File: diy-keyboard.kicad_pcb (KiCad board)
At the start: 2 copper layers, 157 parts, among them J1 AVR-ISP-6, SW1 ESC, SW10 #9, SW11 #0, SW12 -_, SW13 =+, SW14 BCKSPC, SW15 DEL, SW16 TAB, SW17 Q, SW18 W, SW19 E, SW2 #1, SW20 R, SW21 T, SW22 Y, SW23 U, SW24 I, SW25 O, SW26 P, SW27 [{, SW28 ]}, SW29 \|, SW3 #2, SW30 PGUP, SW31 CPSLCK, SW32 A, SW33 S, SW34 D, SW35 F, SW36 G, SW37 H, SW38 J, SW39 K, SW4 #3, SW40 L, SW41 ;:, SW42 '", SW43 ENTR, SW44 PGDN, SW45 LSHFT, SW46 Z, SW47 X, SW48 C, SW49 V, SW5 #4, SW50 B, SW51 N, SW52 M, SW53 ,<, SW54 .>, SW55 /?, SW56 RSHFT, SW57 UP, SW58 INS, SW59 LCTRL, SW6 #5, SW60 SUPER, SW61 LALT, SW62 SPACE, SW63 RALT, SW64 Fn, SW65 RCTRL, SW66 LEFT, SW67 DOWN, SW68 RIGHT, SW69 SW_SKQG, SW7 #6, SW8 #7, SW9 #8, U1 PRTR5V0U2X, U2 ATmega32U4-A, Y1 16MHz

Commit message: Making edge cuts PCB taking a shape
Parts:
- SW69: footprint Button_Switch_SMD:SW_SPST_SKQG_WithoutStem -> Button_Switch_SMD:SW_SPST_SKQG_WithStem
- moved R3 70.1 mm to (153.3, 150.4)
- moved SW69 60.6 mm to (155.4, 155.8)
- moved C7 57.3 mm to (209.2, 149.8), turned to 90 degrees
- moved C5 46.5 mm to (203.5, 148.3), turned to 0 degrees
- moved J1 44.9 mm to (166.5, 155.6)
- moved C4 43.6 mm to (191.9, 151.5), turned to -90 degrees
- moved C6 37.8 mm to (204.2, 164.3), turned to 0 degrees
- moved R6 28.8 mm to (191.0, 162.3)
- moved C8 15.2 mm to (192.7, 148.3)
- moved R5 15.1 mm to (198.9, 146.5)
- moved R4 15.1 mm to (196.9, 146.5)
- moved U2 15.1 mm to (199.9, 156.3)
- moved C2 14.6 mm to (216.6, 154.5)
- moved C1 14.6 mm to (216.6, 156.9)
- moved Y1 14.0 mm to (212.0, 155.9)
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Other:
- board outline added: 304.8 x 98.8 mm

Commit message: Routing switch and diode
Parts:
- added REF**: Stabilizer_Cherry_MX_2.00u, Mounting_Keyboard_Stabilizer:Stabilizer_Cherry_MX_2.00u, F.Cu at (323.1, 81.0)
- added REF**: Stabilizer_Cherry_MX_2.00u, Mounting_Keyboard_Stabilizer:Stabilizer_Cherry_MX_2.00u, F.Cu at (77.8, 138.1)
- added REF**: Stabilizer_Cherry_MX_2.00u, Mounting_Keyboard_Stabilizer:Stabilizer_Cherry_MX_2.00u, F.Cu at (320.7, 119.1)
- added REF**: Stabilizer_Cherry_MX_6.25u, Mounting_Keyboard_Stabilizer:Stabilizer_Cherry_MX_6.25u, F.Cu at (180.2, 157.2)
- moved D8 8.92 mm to (193.9, 84.8)
- moved F1 4.17 mm to (204.6, 86.3), turned to -90 degrees
- moved U1 2.29 mm to (208.7, 84.3)
- moved R2 1.54 mm to (206.2, 79.0)
- moved R1 1.07 mm to (210.9, 79.0)
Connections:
- R4 pad 1: Net-(R4-Pad1) -> /DN
- R4 pad 2: Net-(R4-Pad2) -> /DN
- R5 pad 1: Net-(R5-Pad1) -> /DP
- R5 pad 2: Net-(R5-Pad2) -> /DP
- U1 pad 2: Net-(R5-Pad1) -> /DP
- U1 pad 3: Net-(R4-Pad1) -> /DN
- U2 pad 3: Net-(R4-Pad2) -> /DN
- U2 pad 4: Net-(R5-Pad2) -> /DP
- USB1 pad 5: Net-(R4-Pad1) -> /DN
- USB1 pad 6: Net-(R5-Pad1) -> /DP
- USB1 pad 7: Net-(R4-Pad1) -> /DN
- USB1 pad 8: Net-(R5-Pad1) -> /DP
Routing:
- net /ROW0: track 0.00 -> 292.7 mm, vias 0 -> 2
- net /ROW1: track 0.00 -> 290.3 mm, vias 0 -> 2
- net /ROW2: track 0.00 -> 287.7 mm, vias 0 -> 2
- net /ROW3: track 0.00 -> 281.0 mm, vias 0 -> 2
- net /ROW4: track 0.00 -> 214.2 mm
- net /COL6: track 0.00 -> 108.4 mm
- net /COL1: track 0.00 -> 100.9 mm
- net /COL2: track 0.00 -> 99.6 mm
- net /DN: track 0.00 -> 89.8 mm
- net /COL9: track 0.00 -> 89.5 mm
- net /COL10: track 0.00 -> 88.6 mm
- net /DP: track 0.00 -> 88.4 mm
- net /COL13: track 0.00 -> 87.1 mm
- net /COL0: track 0.00 -> 85.6 mm
- net /COL12: track 0.00 -> 84.1 mm
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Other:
- board size 304.8 x 98.8 mm -> 304.8 x 99.9 mm

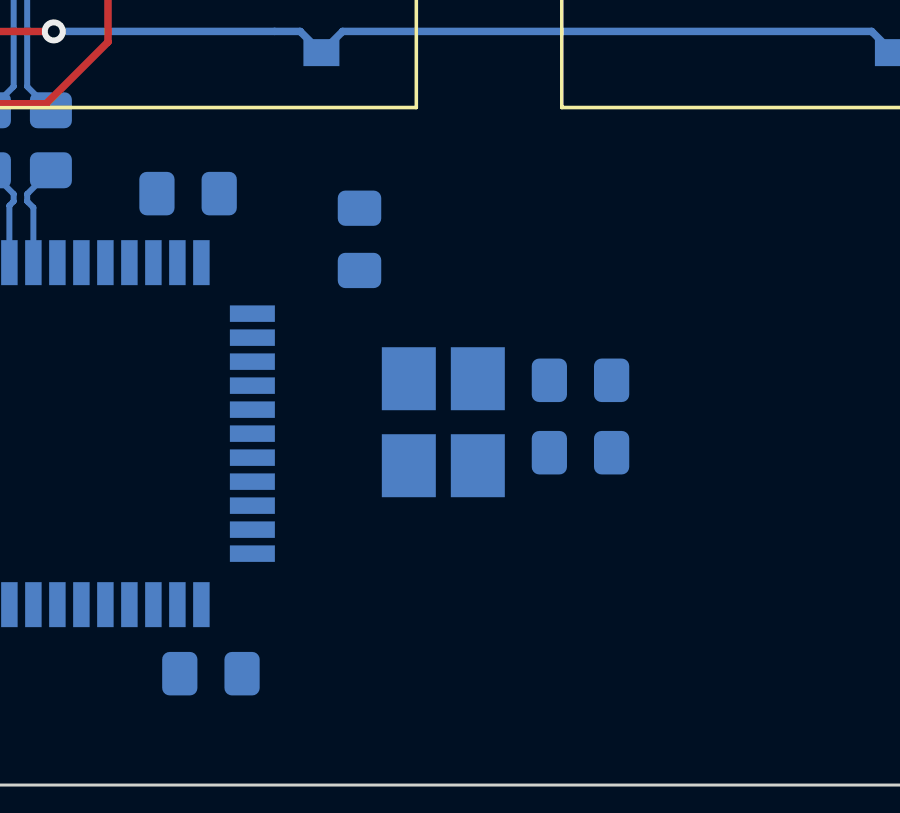
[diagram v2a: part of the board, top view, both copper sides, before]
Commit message: Routing USB and Crystal Oscillator
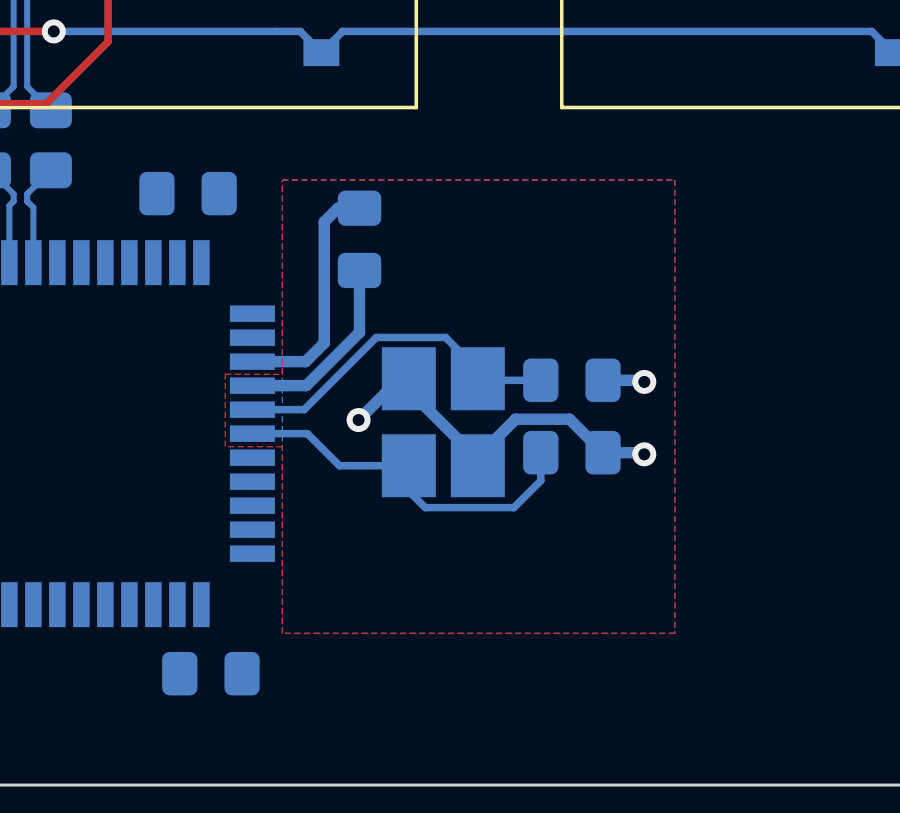
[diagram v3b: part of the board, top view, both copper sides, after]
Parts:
- moved C1 0.29 mm to (216.3, 156.9)
- moved C2 0.29 mm to (216.3, 154.5)
- turned C7 to -90 degrees
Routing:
- net GND: track 0.00 -> 21.0 mm, vias 0 -> 3
- net Net-(C1-Pad1): track 0.00 -> 12.4 mm
- net Net-(C2-Pad1): track 0.00 -> 11.4 mm
- net +5V: track 0.00 -> 8.05 mm
- added copper zone on B.Cu, net GND
- added copper zone on F.Cu, net GND

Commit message: Reassign footprint SW59 and re-allign keyboard layout
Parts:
- SW59: footprint Switch_Keyboard_Cherry_MX:SW_Cherry_MX_PCB_1.25u -> Switch_Keyboard_Cherry_MX:SW_Cherry_MX_PCB_1.50u
- SW63: footprint Switch_Keyboard_Cherry_MX:SW_Cherry_MX_PCB_1.25u -> Switch_Keyboard_Cherry_MX:SW_Cherry_MX_PCB_1.00u
- moved SW69 71.3 mm to (226.6, 152.9)
- moved R3 65.8 mm to (219.1, 151.0)
- moved R6 7.42 mm to (198.2, 164.3)
- moved C6 6.23 mm to (210.5, 164.5)
- moved C3 5.99 mm to (195.6, 161.3), turned to 180 degrees
- moved C7 5.60 mm to (214.7, 151.0), turned to 0 degrees
- moved D61 5.56 mm to (118.2, 161.2)
- moved D60 5.51 mm to (99.1, 161.2)
- moved D62 5.50 mm to (189.3, 161.1)
- moved REF** 4.77 mm to (184.9, 157.4)
- moved SW60 4.76 mm to (94.5, 157.4)
- moved SW61 4.76 mm to (113.5, 157.4)
- moved SW62 4.76 mm to (184.9, 157.4)
- moved R5 4.48 mm to (203.4, 147.1)
- moved R4 4.48 mm to (201.3, 147.1)
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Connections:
- R4 pad 2: /DN -> /D-
- R5 pad 2: /DP -> /D+
- U2 pad 3: /DN -> /D-
- U2 pad 36: /COL6 -> /ROW4
- U2 pad 37: /COL5 -> /COL6
- U2 pad 38: /ROW1 -> /COL5
- U2 pad 39: /ROW4 -> /ROW3
- U2 pad 4: /DP -> /D+
- U2 pad 40: /ROW3 -> /ROW2
- U2 pad 41: /ROW2 -> /ROW1
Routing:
- net /ROW4: track 214.2 -> 296.7 mm, vias 0 -> 2
- net /DP: track 88.4 -> 12.9 mm
- net /DN: track 89.8 -> 14.5 mm
- net GND: track 21.0 -> 93.8 mm, vias 3 -> 0
- net /RESET: track 0.00 -> 25.3 mm
- net /COL1: track 100.9 -> 88.9 mm
- net /COL2: track 99.6 -> 88.9 mm
- net Net-(C2-Pad1): track 11.4 -> 2.05 mm
- net +5V: track 8.05 -> 16.7 mm
- net /ROW0: track 292.7 -> 300.8 mm
- net /COL14: track 78.3 -> 71.1 mm
- net Net-(C1-Pad1): track 12.4 -> 5.86 mm
- net /ROW3: track 281.0 -> 286.2 mm
- net /COL9: track 89.5 -> 85.0 mm
- net /COL0: track 85.6 -> 81.0 mm
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- removed copper zone on B.Cu, net GND
- removed copper zone on F.Cu, net GND

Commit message: Change diode footprint to 1N4148 SOD-123 and re-routing PCB
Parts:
- removed REF** (x3): Stabilizer_Cherry_MX_2.00u, Mounting_Keyboard_Stabilizer:Stabilizer_Cherry_MX_2.00u
- removed REF**: Stabilizer_Cherry_MX_6.25u, Mounting_Keyboard_Stabilizer:Stabilizer_Cherry_MX_6.25u
- added H1: MountingHole, Local_lib_Mounting_Keyboard_Stabilizer:Stabilizer_Cherry_MX_6.25u, F.Cu at (182.6, 165.1)
- added H2: MountingHole, Local_lib_Mounting_Keyboard_Stabilizer:Stabilizer_Cherry_MX_2.00u, F.Cu at (320.6, 88.9)
- added H3: MountingHole, Local_lib_Mounting_Keyboard_Stabilizer:Stabilizer_Cherry_MX_2.00u, F.Cu at (318.3, 127.0)
- added H4: MountingHole, Local_lib_Mounting_Keyboard_Stabilizer:Stabilizer_Cherry_MX_2.00u, F.Cu at (75.4, 146.1)
- D1, D10, D11, D12, D13, D14, D15, D16, D17, D18, D19, D2, D20, D21, D22, D23, D24, D25, D26, D27, D28, D29, D3, D30, D31, D32, D33, D34, D35, D36, D37, D38, D39, D4, D40, D41, D42, D43, D44, D45, D46, D47, D48, D49, D5, D50, D51, D52, D53, D54, D55, D56, D57, D58, D59, D6, D60, D61, D62, D63, D64, D65, D66, D67, D68, D7, D8, D9: value D -> 1N4148W
- J1: footprint ISP-header:Reset_Pretty-Mask -> Local_lib_ISP-header:Reset_Pretty-Mask; moved to F.Cu
- SW1, SW10, SW11, SW12, SW13, SW15, SW17, SW18, SW19, SW2, SW20, SW21, SW22, SW23, SW24, SW25, SW26, SW27, SW28, SW3, SW30, SW32, SW33, SW34, SW35, SW36, SW37, SW38, SW39, SW4, SW40, SW41, SW42, SW44, SW46, SW47, SW48, SW49, SW5, SW50, SW51, SW52, SW53, SW54, SW55, SW57, SW58, SW6, SW60, SW61, SW63, SW64, SW65, SW66, SW67, SW68, SW7, SW8, SW9: footprint Switch_Keyboard_Cherry_MX:SW_Cherry_MX_PCB_1.00u -> Local_lib_Switch_Keyboard_Cherry_MX:SW_Cherry_MX_PCB_1.00u
- SW14: footprint Switch_Keyboard_Cherry_MX:SW_Cherry_MX_PCB_2.00u -> Local_lib_Switch_Keyboard_Cherry_MX:SW_Cherry_MX_PCB_2.00u
- SW16, SW29, SW59: footprint Switch_Keyboard_Cherry_MX:SW_Cherry_MX_PCB_1.50u -> Local_lib_Switch_Keyboard_Cherry_MX:SW_Cherry_MX_PCB_1.50u
- SW31, SW56: footprint Switch_Keyboard_Cherry_MX:SW_Cherry_MX_PCB_1.75u -> Local_lib_Switch_Keyboard_Cherry_MX:SW_Cherry_MX_PCB_1.75u
- SW43, SW45: footprint Switch_Keyboard_Cherry_MX:SW_Cherry_MX_PCB_2.25u -> Local_lib_Switch_Keyboard_Cherry_MX:SW_Cherry_MX_PCB_2.25u
- SW62: footprint Switch_Keyboard_Cherry_MX:SW_Cherry_MX_PCB_6.50u -> Local_lib_Switch_Keyboard_Cherry_MX:SW_Cherry_MX_PCB_6.50u
- U1: footprint Package_TO_SOT_SMD:SOT-143_Handsoldering -> Package_TO_SOT_SMD:SOT-143
- USB1: footprint Type-C:HRO-TYPE-C-31-M-12-HandSoldering -> Local_lib_Type-C:HRO-TYPE-C-31-M-12-HandSoldering
- moved J1 70.5 mm to (240.4, 163.7), turned to 0 degrees
- moved C7 25.7 mm to (191.0, 161.0), turned to 180 degrees
- moved C4 23.6 mm to (205.6, 173.5)
- moved R1 23.0 mm to (189.4, 86.9), turned to -90 degrees
- moved U1 22.5 mm to (187.3, 91.3)
- moved R2 22.5 mm to (184.9, 86.0)
- moved USB1 22.3 mm to (187.3, 73.3)
- moved F1 22.0 mm to (183.5, 92.7)
- moved D7 13.7 mm to (172.7, 92.8)
- moved SW69 13.3 mm to (224.2, 166.0)
- moved R3 11.4 mm to (221.7, 162.1)
- moved C1 11.1 mm to (215.4, 167.6)
- moved Y1 10.7 mm to (211.1, 166.1)
- moved C2 10.7 mm to (215.4, 164.7)
- moved D8 10.6 mm to (200.8, 92.8)
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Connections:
- U2 pad 1: /ROW0 -> /COL5
- U2 pad 38: /COL5 -> /ROW0
- U2 pad 39: /ROW3 -> /ROW1
- U2 pad 41: /ROW1 -> /ROW3
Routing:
- net /ROW0: track 300.8 -> 500.6 mm
- net GND: track 93.8 -> 281.6 mm, vias 0 -> 42
- net /ROW1: track 293.9 -> 480.1 mm
- net +5V: track 16.7 -> 191.9 mm, vias 0 -> 9
- net /COL14: track 71.1 -> 228.8 mm, vias 0 -> 1
- net /ROW2: track 291.9 -> 448.4 mm
- net /COL0: track 81.0 -> 227.8 mm, vias 0 -> 1
- net /COL13: track 82.6 -> 219.8 mm, vias 0 -> 1
- net /COL1: track 88.9 -> 209.8 mm, vias 0 -> 1
- net /COL12: track 81.4 -> 199.1 mm, vias 0 -> 1
- net /COL2: track 88.9 -> 188.5 mm, vias 0 -> 1
- net /COL11: track 81.4 -> 173.7 mm, vias 0 -> 1
- net /COL3: track 64.3 -> 144.6 mm, vias 0 -> 1
- net /DP: track 12.9 -> 85.7 mm
- net /COL10: track 85.0 -> 156.4 mm, vias 0 -> 1
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- added copper zone on B.Cu, net GND
- added copper zone on F.Cu, net GND
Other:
- board size 304.8 x 99.9 mm -> 304.8 x 101.7 mm

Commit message: Re-assign symbol and footprint to match local library
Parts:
- H1: footprint Local_lib_Mounting_Keyboard_Stabilizer:Stabilizer_Cherry_MX_6.25u -> Local_Lib:Stabilizer_Cherry_MX_6.25u
- H2, H3, H4: footprint Local_lib_Mounting_Keyboard_Stabilizer:Stabilizer_Cherry_MX_2.00u -> Local_Lib:Stabilizer_Cherry_MX_2.00u
- J1: footprint Local_lib_ISP-header:Reset_Pretty-Mask -> Local_Lib:Reset_Pretty-Mask
- SW1, SW10, SW11, SW12, SW13, SW15, SW17, SW18, SW19, SW2, SW20, SW21, SW22, SW23, SW24, SW25, SW26, SW27, SW28, SW3, SW30, SW32, SW33, SW34, SW35, SW36, SW37, SW38, SW39, SW4, SW40, SW41, SW42, SW44, SW46, SW47, SW48, SW49, SW5, SW50, SW51, SW52, SW53, SW54, SW55, SW57, SW58, SW6, SW60, SW61, SW63, SW64, SW65, SW66, SW67, SW68, SW7, SW8, SW9: footprint Local_lib_Switch_Keyboard_Cherry_MX:SW_Cherry_MX_PCB_1.00u -> Local_Lib:SW_Cherry_MX_PCB_1.00u
- SW14: footprint Local_lib_Switch_Keyboard_Cherry_MX:SW_Cherry_MX_PCB_2.00u -> Local_Lib:SW_Cherry_MX_PCB_2.00u
- SW16, SW29, SW59: footprint Local_lib_Switch_Keyboard_Cherry_MX:SW_Cherry_MX_PCB_1.50u -> Local_Lib:SW_Cherry_MX_PCB_1.50u
- SW31, SW56: footprint Local_lib_Switch_Keyboard_Cherry_MX:SW_Cherry_MX_PCB_1.75u -> Local_Lib:SW_Cherry_MX_PCB_1.75u
- SW43, SW45: footprint Local_lib_Switch_Keyboard_Cherry_MX:SW_Cherry_MX_PCB_2.25u -> Local_Lib:SW_Cherry_MX_PCB_2.25u
- SW62: footprint Local_lib_Switch_Keyboard_Cherry_MX:SW_Cherry_MX_PCB_6.50u -> Local_Lib:SW_Cherry_MX_PCB_6.50u
- USB1: footprint Local_lib_Type-C:HRO-TYPE-C-31-M-12-HandSoldering -> Local_Lib:HRO-TYPE-C-31-M-12-HandSoldering

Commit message: Routing usb shield to ferrite bead
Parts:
- added FB1: 60@100MHz, Inductor_SMD:L_0805_2012Metric_Pad1.15x1.40mm_HandSolder, B.Cu at (196.2, 80.6)
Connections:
- USB1 pad 13: GND -> Earth
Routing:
- net GND: track 281.6 -> 260.6 mm, vias 42 -> 43
- net Earth: vias 0 -> 4
- added copper zone on B.Cu, net Earth
- added copper zone on F.Cu, net Earth

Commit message: Add kicad logo
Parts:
- added REF**: KiCad-Logo2_5mm_SilkScreen, Symbol:KiCad-Logo2_5mm_SilkScreen, F.Cu at (206.5, 165.1)
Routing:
- net /ROW2: track 448.4 -> 471.9 mm
- net /ROW1: track 480.1 -> 494.0 mm
- net /ROW0: track 500.6 -> 514.4 mm
